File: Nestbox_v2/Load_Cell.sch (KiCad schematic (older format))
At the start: 18 parts

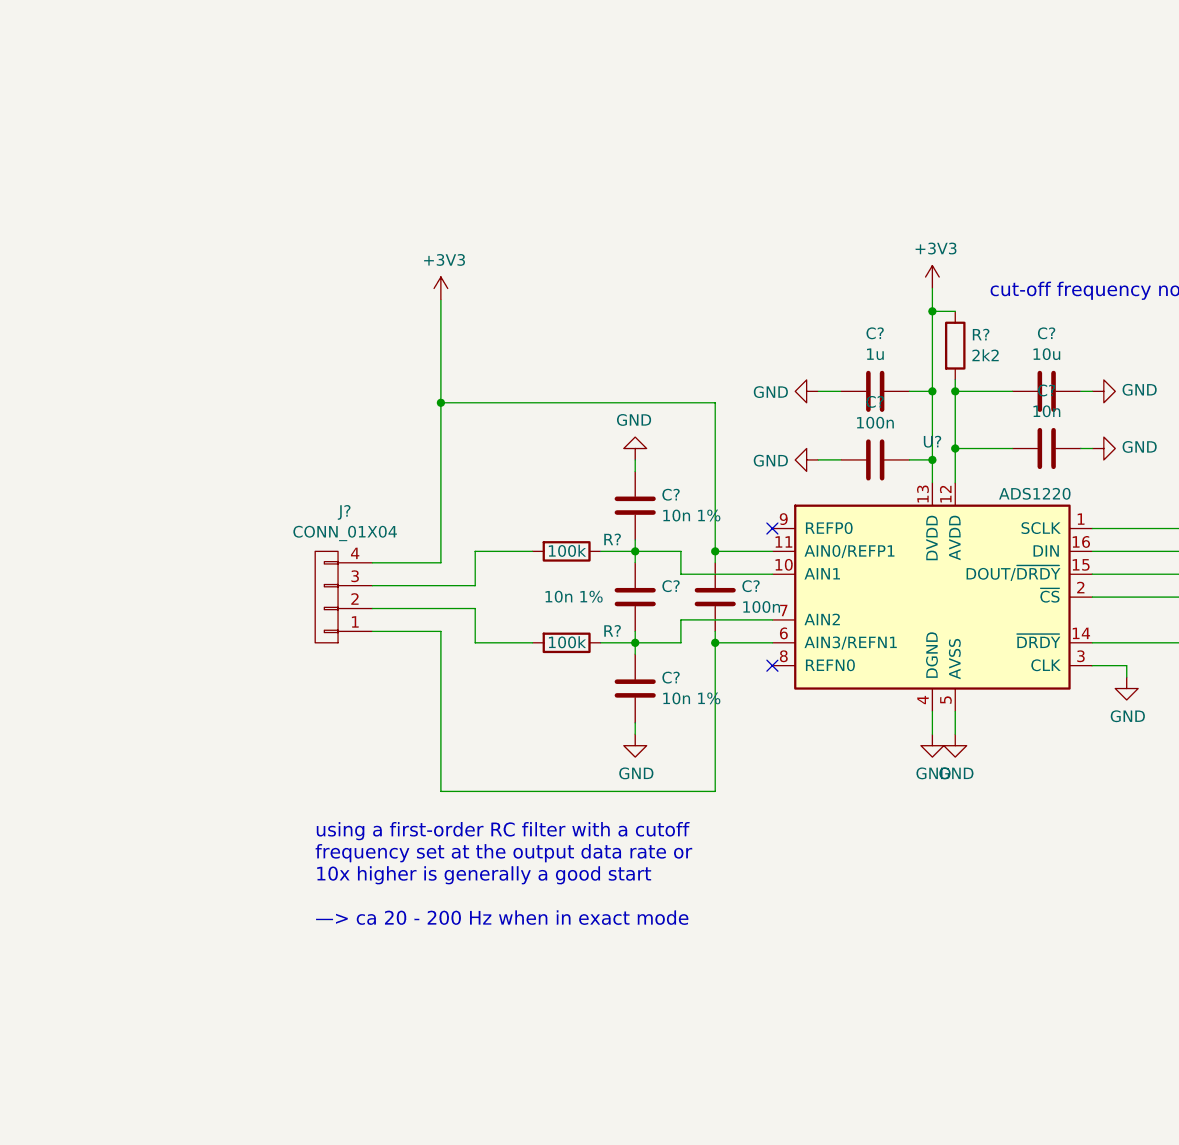
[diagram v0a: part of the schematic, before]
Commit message: more comments on ADC
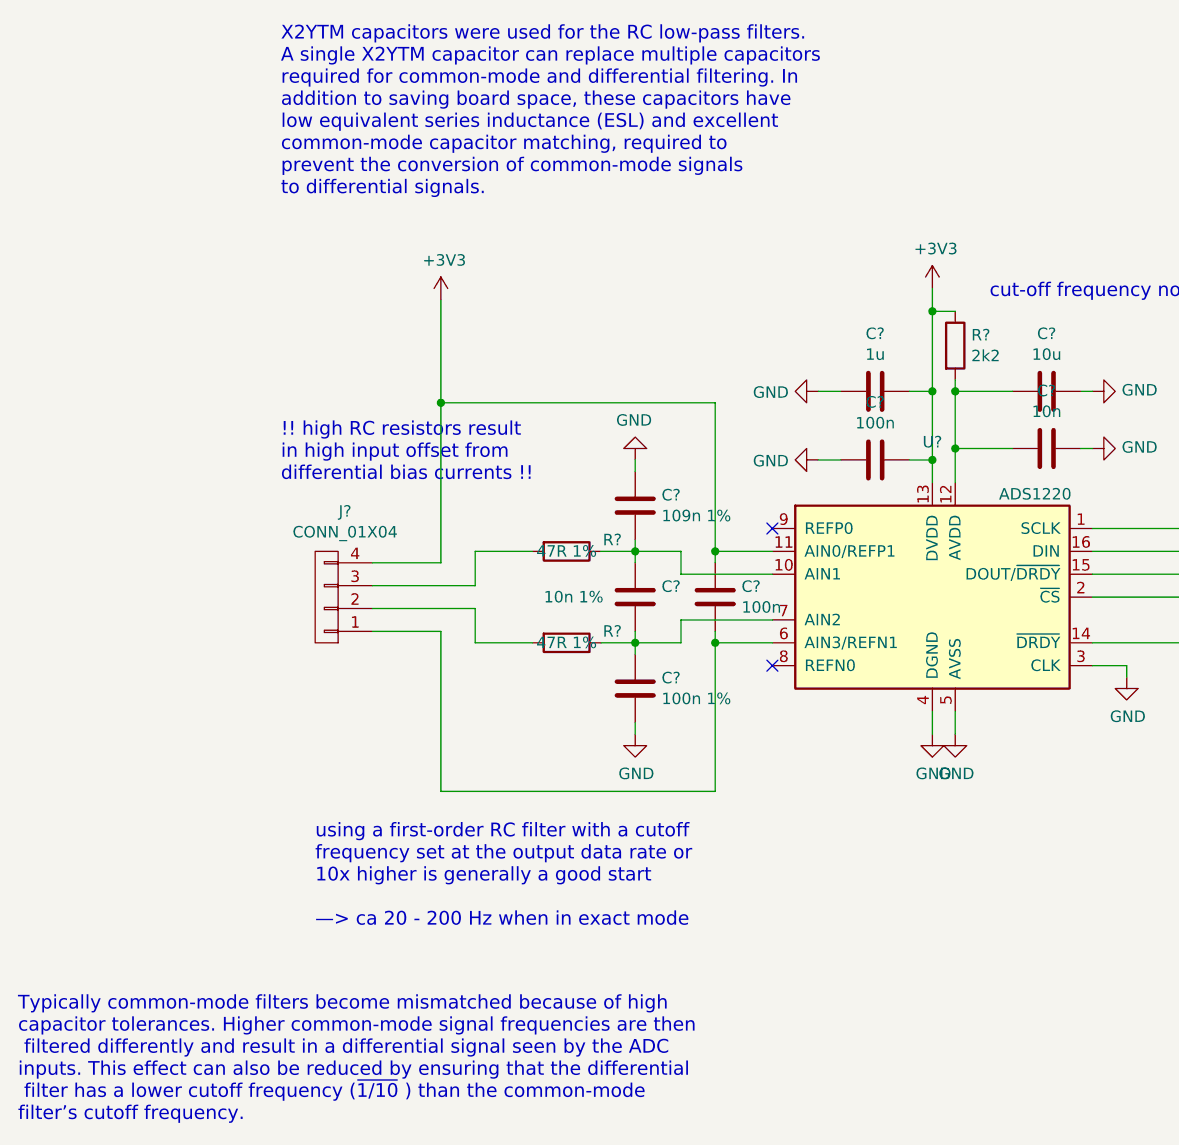
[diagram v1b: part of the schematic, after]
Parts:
- C?: value 10n 1% -> 100n 1%
- C?: value 10n 1% -> 109n 1%
- R? (x2): value 100k -> 47R 1%
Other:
- note added: "!! high RC resistors result \nin high input offset from \ndifferential bias currents !!"
- note added: "Typically common-mode filters become mismatched because of high \ncapacitor tolerances. Higher common-mode signal frequencies are then\n filtered differently and result in a differential signal seen by the ADC \ninputs. This effect can also be reduced by ensuring that the differential\n filter has a lower cutoff frequency (~1/10 ) than the common-mode \nfilter’s cutoff frequency. \n"
- note added: "X2YTM capacitors were used for the RC low-pass filters. \nA single X2YTM capacitor can replace multiple capacitors \nrequired for common-mode and differential filtering. In \naddition to saving board space, these capacitors have \nlow equivalent series inductance (ESL) and excellent \ncommon-mode capacitor matching, required to \nprevent the conversion of common-mode signals \nto differential sig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"
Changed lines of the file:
@@
 P 4250 4400
 F 0 "C?" H 4365 4446 50  0000 L CNN
-F 1 "10n 1%" H 4365 4355 50  0000 L CNN
+F 1 "100n 1%" H 4365 4355 50  0000 L CNN
 F 2 "" H 4288 4250 50  0001 C CNN
 F 3 "" H 4250 4400 50  0001 C CNN
@@
 P 4250 3600
 F 0 "C?" H 4365 3646 50  0000 L CNN
-F 1 "10n 1%" H 4365 3555 50  0000 L CNN
+F 1 "109n 1%" H 4365 3555 50  0000 L CNN
 F 2 "" H 4288 3450 50  0001 C CNN
 F 3 "" H 4250 3600 50  0001 C CNN
@@
 P 3950 3800
 F 0 "R?" V 3900 4000 50  0000 C CNN
-F 1 "100k" V 3950 3800 50  0000 C CNN
+F 1 "47R 1%" V 3950 3800 50  0000 C CNN
 F 2 "" V 3880 3800 50  0001 C CNN
 F 3 "" H 3950 3800 50  0001 C CNN
@@
 P 3950 4200
 F 0 "R?" V 3900 4400 50  0000 C CNN
-F 1 "100k" V 3950 4200 50  0000 C CNN
+F 1 "47R 1%" V 3950 4200 50  0000 C CNN
 F 2 "" V 3880 4200 50  0001 C CNN
 F 3 "" H 3950 4200 50  0001 C CNN
@@
 Text Notes 2850 5450 0    60   ~ 0
 using a first-order RC filter with a cutoff \nfrequency set at the output data rate or \n10x higher is generally a good start\n\n—> ca 20 - 200 Hz when in exact mode\n
+Text Notes 2700 2250 0    60   ~ 0
+X2YTM capacitors were used for the RC low-pass filters. \nA single X2YTM capacitor can replace multiple capacitors \nrequired for common-mode and differential filtering. In \naddition to saving board space, these capacitors have \nlow equivalent series inductance (ESL) and excellent \ncommon-mode capacitor matching, required to \nprevent the conversion of common-mode signals \nto differential signals. \n
+Text Notes 2700 3500 0    60   ~ 0
+!! high RC resistors result \nin high input offset from \ndifferential bias currents !!
+Text Notes 1550 6300 0    60   ~ 0
+Typically common-mode filters become mismatched because of high \ncapacitor tolerances. Higher common-mode signal frequencies are then\n filtered differently and result in a differential signal seen by the ADC \ninputs. This effect can also be reduced by ensuring that the differential\n filter has a lower cutoff frequency (~1/10 ) than the common-mode \nfilter’s cutoff frequency. \n
 $EndSCHEMATC

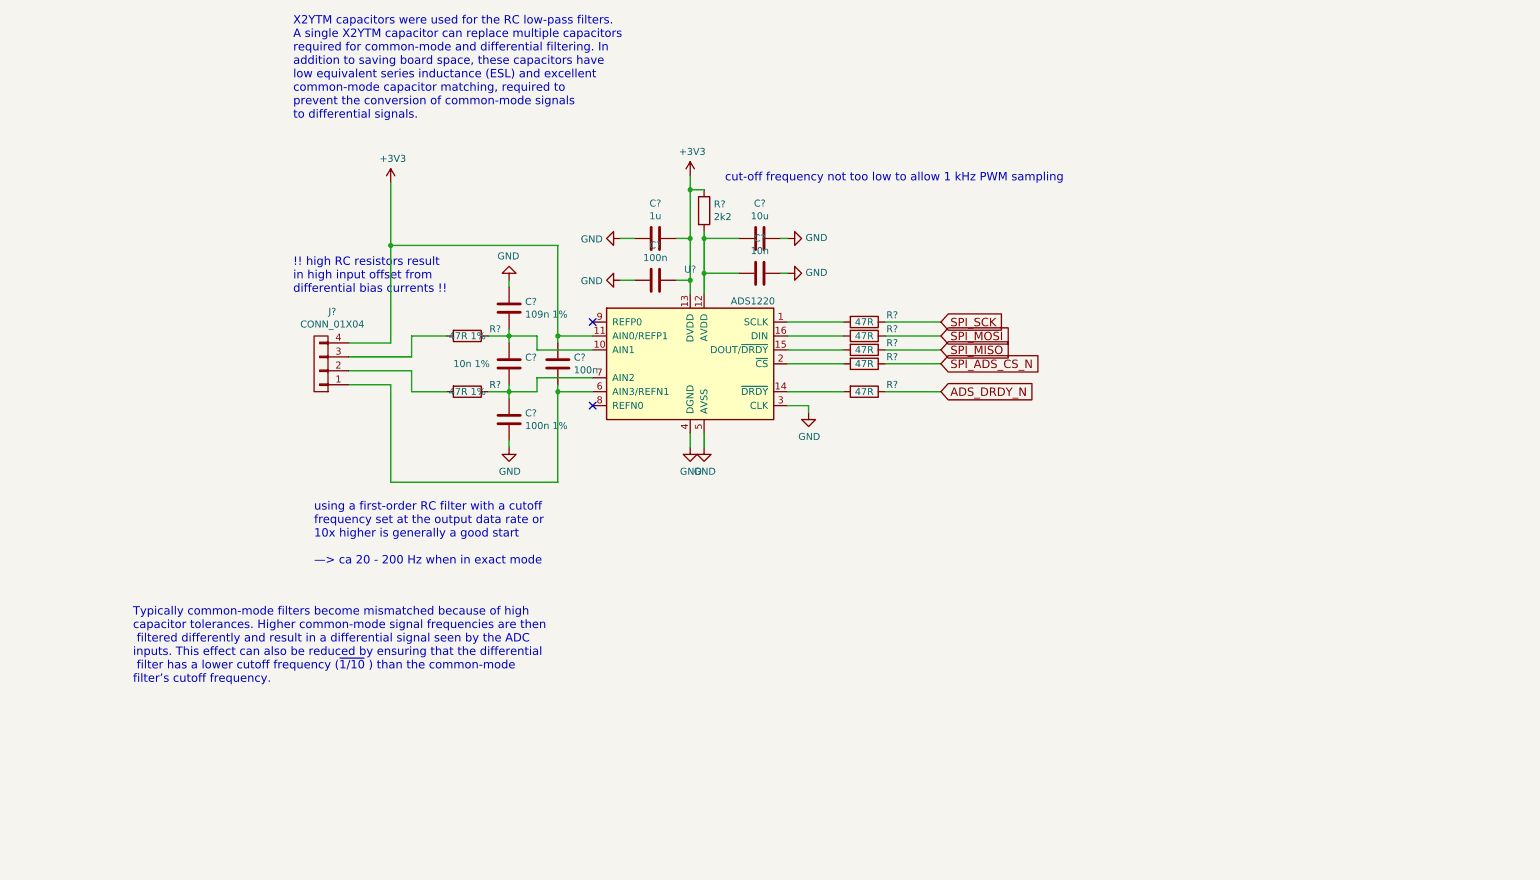
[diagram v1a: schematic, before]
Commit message: load cell AC excitation
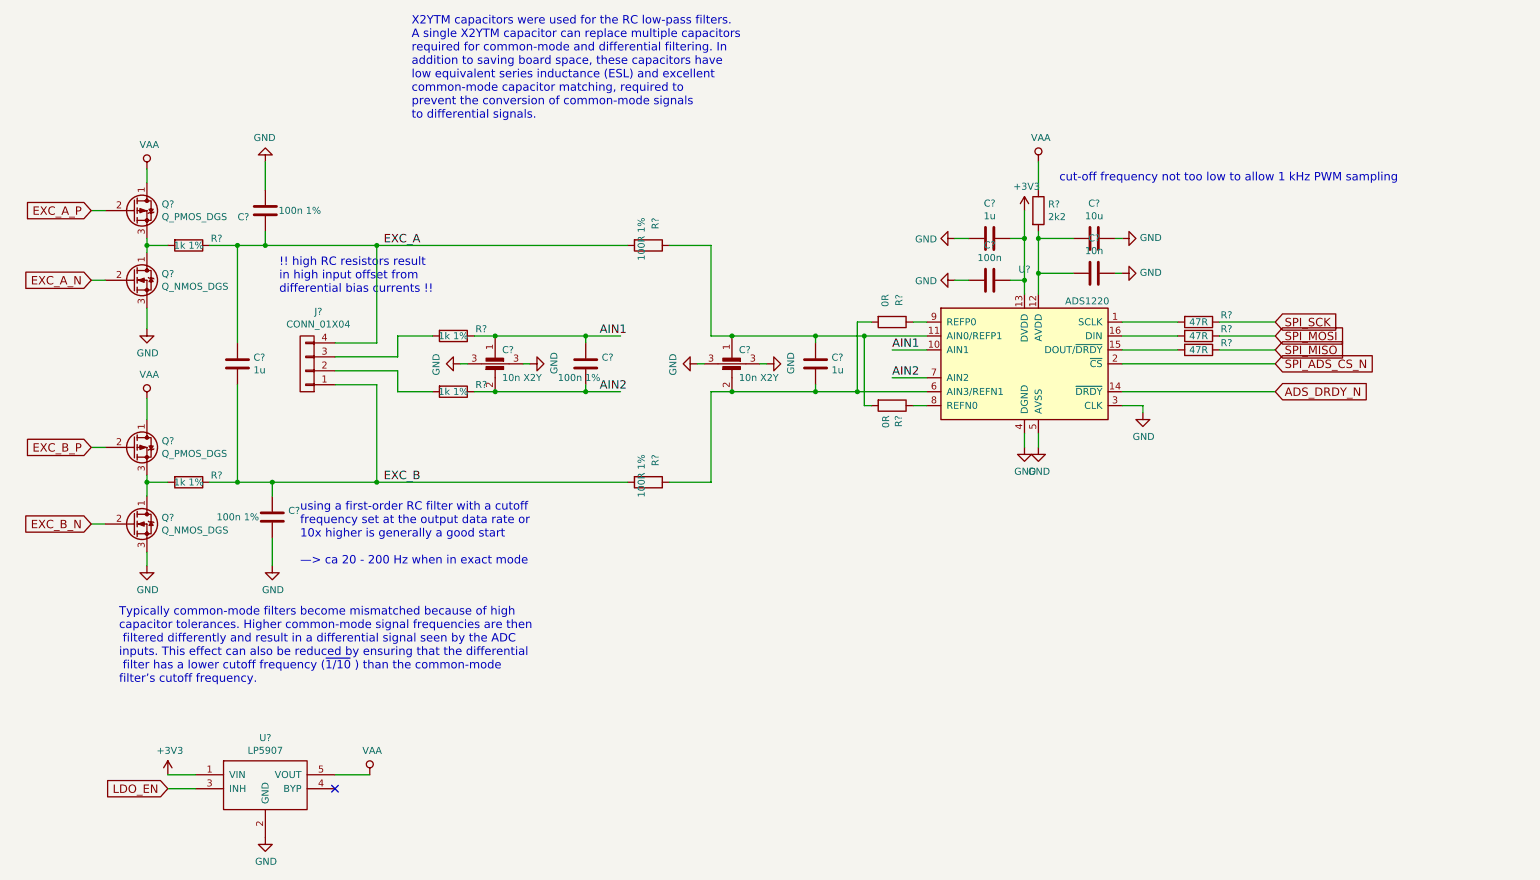
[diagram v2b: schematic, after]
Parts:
- removed C?: 100n 1%, symbol C
- removed C?: 109n 1%, symbol C
- removed R? (x2): 47R, symbol R
- added C? (x2): 100n 1%, symbol C
- added C?: 1u, symbol C
- added C? (x2): 10n X2Y, symbol C_X2Y
- added Q? (x2): Q_NMOS_DGS, symbol Q_NMOS_DGS
- added Q? (x2): Q_PMOS_DGS, symbol Q_PMOS_DGS
- added R? (x2): 1k 1%, symbol R
- added R? (x2): 0R, symbol R
- added R? (x2): 100R 1%, symbol R
- added U?: LP5907, TO_SOT_Packages_SMD:SOT-23-5, symbol LD3985M
- C?: value 10n 1% -> 100n 1%
- C?: value 100n -> 1u
- R? (x2): value 47R 1% -> 1k 1%
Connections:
- net +3V3: now also U?.1 (VIN); no longer C?.1, J?.4 (P4), R?.1, U?.11 (AIN0/REFP1)
- net ADS_DRDY_N: now also U?.14 (~DRDY)
- net GND: now also C?.2, C?.2, C?.3, C?.3, Q?.3 (S), Q?.3 (S), U?.2 (GND)
- net SPI_ADS_CS_N: now also U?.2 (~CS)
- net AIN1: now reaches C?.1, R?.1, U?.10 (AIN1)
- net AIN1: now also C?.1
- net at C?.2, U?.6 (AIN3/REFN1): now also C?.2, R?.1, R?.2; no longer J?.1 (P1)
- net AIN2: now reaches C?.2, R?.1, U?.7 (AIN2)
- net AIN2: now also C?.2
- net at U?.8 (REFN0): now also R?.1
- net at U?.9 (REFP0): now also R?.1
- new net: C?.1, C?.1, R?.1, R?.2, U?.11 (AIN0/REFP1)
- new net: Q?.1 (D), Q?.3 (S), R?.2 (x2)
- new net EXC_A: C?.1, C?.1, J?.4 (P4), R?.1, R?.2
- new net EXC_A_N: Q?.2 (G)
- new net EXC_A_P: Q?.2 (G)
- new net EXC_B: C?.1, C?.2, J?.1 (P1), R?.1, R?.2
- new net EXC_B_N: Q?.2 (G)
- new net EXC_B_P: Q?.2 (G)
- new net LDO_EN: U?.3 (INH)
- new net VAA: Q?.1 (D), Q?.1 (D), R?.1, U?.5 (VOUT)
- no-connect marks 2 -> 1
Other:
- moved on the sheet: C?, J?, R?, U?
